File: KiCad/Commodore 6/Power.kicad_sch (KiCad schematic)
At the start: 49 parts, among them J3 Conn_01x05_Pin, Q1 NTR4501NT1G, Q2 PMOS, SW2 SWITCH, SW4 SWITCH, SW6 SWITCH

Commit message: power
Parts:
- removed 1.8LDO: LP5907MFX-1.8, Package_TO_SOT_SMD:SOT-23-5, symbol Regulator_Linear:LP5907MFX-1.8
- removed 2.8LDO: LP5907MFX-2.8, Package_TO_SOT_SMD:SOT-23-5, symbol Regulator_Linear:LP5907MFX-2.8
- removed 3.3LDO: TLV75533PDBV, Package_TO_SOT_SMD:SOT-23-5, symbol Regulator_Linear:TLV75533PDBV
- removed C22, C23, C26, C27, C34, C35: 1uf, symbol Device:C
- removed D1, D3, D4: LED(red), symbol Device:LED
- removed D5: D_Zener_Filled, symbol Device:D_Zener_Filled
- removed DSUB: DA15_Pins, symbol Connector:DA15_Pins
- removed R12, R4: 100R, symbol Device:R
- removed R21: 70R, symbol Device:R
- removed SW2, SW4, SW6: SWITCH, symbol Switch:SW_DPST_x2
- added J4: DE15_Socket_HighDensity_MountingHoles, symbol Connector:DE15_Socket_HighDensity_MountingHoles
- added schottkey: PDS1040L-13, PDS1040L-13:DIO_PDS1040L-13, symbol PDS1040L-13:PDS1040L-13
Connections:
- net 8.4V_evil: now also Q2.1 (D); no longer Q2.3 (S)
- net GND: now also J4.11, J4.12, J4.3, J4.4
- net GNDD: no longer BatteryConnector.2, BatteryConnector.3, C32.1, R13.1, R14.1, R15.1, R16.2
- net RXD: now also J4.15
- net TXD: now also J4.8
- net VOUT: now also BatteryConnector.3, C32.1, R15.1, R16.2, J4.1, J4.10, J4.2, J4.9, schottkey.1, schottkey.2
- net at C33.1, R18.1: now also Q2.3 (S), schottkey.3; no longer Q2.1 (D)
- new net: BatteryConnector.2, R13.1, R14.1
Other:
- added sheet chud ldos (LDOs.kicad_sch)
- moved on the sheet: J3, Q2, TestPoint

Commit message: more
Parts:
- removed C36: 1uF, symbol Device:C
- removed J3: Conn_01x05_Pin, symbol Connector:Conn_01x05_Pin
- removed J4: DE15_Socket_HighDensity_MountingHoles, symbol Connector:DE15_Socket_HighDensity_MountingHoles
- removed TestPoint: GND, symbol Connector:TestPoint
- added C36: WCAP-ASLL_4X5.5/865060640001 1uf smd electrolytic, WCAP-ASLL_4X5.5:WCAP-ASLL_4X5.5_DXL_, symbol WCAP-ASLL_4X5.5:WCAP-ASLL_4X5.5
- added DSUB: ICD15S13E4GX00LF, ICD15S13E4GX00LF:AMPHENOL_ICD15S13E4GX00LF, symbol ICD15S13E4GX00LF:ICD15S13E4GX00LF
- added J6: 6130XX11121_61300511121, 6130XX11121_61300511121:61300511121, symbol 6130XX11121_61300511121:6130XX11121_61300511121
- added R26: RC0402JR-071KL 1k, RC0402N_YAG, symbol 2025-10-26_18-21-17:RC0402JR-071KL
- added TP1: RCWCTE, RCWCTE:TP420X150, symbol RCWCTE:RCWCTE
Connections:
- net 1.8V: now also J6.1
- net 2.8V: now also J6.2
- net 3.3V: now also J6.3
- net 5V: now also C36.1, J6.4
- net 8.4V: now also J6.5
- net GND: now also DSUB.11, DSUB.12, DSUB.3, DSUB.4
- net GNDA: now also TP1.1
- net GNDD: now also C36.2, R26.2
- net RXD: now also DSUB.15
- net TXD: now also DSUB.8
- net VOUT: now also DSUB.1, DSUB.10, DSUB.2, DSUB.9
- net at Payload_Header.2, Payload_LoadSwitch.6 (VOUT): now also R26.1
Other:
- moved on the sheet: Payload_Header

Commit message: AAAAAAAAAA
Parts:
- removed R22: 10k, symbol Device:R
- added C39: WCAP-ASLI_5X5.5/ 47uf electro, WCAP-ASLI_5X5.5:WCAP-ASLI_5X5.5_DXL_, symbol WCAP-ASLI_5X5.5:WCAP-ASLI_5X5.5
- added R27: RC0201FR-0710KL/ 10k, YAG_R0201_YAG, symbol 2025-10-26_02-06-39:RC0201FR-0710KL
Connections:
- net GNDD: now also C39.2, R27.1
- net Payload_Switch: now also R27.2
- net at Payload_Header.2, Payload_LoadSwitch.6 (VOUT), R26.1: now also C39.1
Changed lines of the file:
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@@
 	)
 	(junction
-		(at 130.81 157.48)
+		(at 40.64 39.37)
 		(diameter 0)
 		(color 0 0 0 0)
 	)
 	(junction
-		(at 81.28 34.29)
+		(at 130.81 157.48)
 		(diameter 0)
 		(color 0 0 0 0)
 	)
 	(junction
-		(at 99.06 34.29)
+		(at 81.28 34.29)
 		(diameter 0)
 		(color 0 0 0 0)
 	)
 	(junction
-		(at 40.64 39.37)
+		(at 99.06 34.29)
 		(diameter 0)
 		(color 0 0 0 0)
@@
 	)
 	(junction
+		(at 92.71 34.29)
+		(diameter 0)
+		(color 0 0 0 0)
+	)
+	(junction
 		(at 72.39 154.94)
 		(diameter 0)
@@
 	(wire
 		(pts
+			(xy 92.71 34.29) (xy 99.06 34.29)
+		)
+		(stroke
+			(width 0)
+			(type default)
+		)
+	)
+	(wire
+		(pts
 			(xy 64.77 74.93) (xy 64.77 87.63)
 		)
@@
 	(wire
 		(pts
-			(xy 81.28 34.29) (xy 99.06 34.29)
+			(xy 40.64 52.07) (xy 40.64 53.34)
+		)
+		(stroke
+			(width 0)
+			(type default)
+		)
+	)
+	(wire
+		(pts
+			(xy 81.28 34.29) (xy 92.71 34.29)
 		)
 		(stroke
@@
 	(wire
 		(pts
+			(xy 40.64 39.37) (xy 45.72 39.37)
+		)
+		(stroke
+			(width 0)
+			(type default)
+		)
+	)
+	(wire
+		(pts
 			(xy 72.39 162.56) (xy 72.39 177.8)
 		)
@@
 	(wire
 		(pts
-			(xy 40.64 39.37) (xy 45.72 39.37)
-		)
-		(stroke
-			(width 0)
-			(type default)
-		)
-	)
-	(wire
-		(pts
 			(xy 80.01 157.48) (xy 80.01 167.64)
 		)
@@
 	)
 	(symbol
+		(lib_id "power:GNDD")
+		(at 92.71 41.91 0)
+		(unit 1)
+		(exclude_from_sim no)
+		(in_bom yes)
+		(on_board yes)
+		(dnp no)
+		(fields_autoplaced yes)
+		(property "Reference" "#PWR0105"
+			(at 92.71 48.26 0)
+			(effects
+				(font
+					(size 1.27 1.27)
+				)
+				(hide yes)
+			)
+		)
+		(property "Value" "GNDD"
+			(at 92.71 45.72 0)
+			(effects
+				(font
+					(size 1.27 1.27)
+				)
+			)
+		)
+		(property "Footprint" ""
+			(at 92.71 41.91 0)
+			(effects
+				(font
+					(size 1.27 1.27)
+				)
+				(hide yes)
+			)
+		)
+		(property "Datasheet" ""
+			(at 92.71 41.91 0)
+			(effects
+				(font
+					(size 1.27 1.27)
+				)
+				(hide yes)
+			)
+		)
+		(property "Description" "Power symbol creates a global label with name \"GNDD\" , digital ground"
+			(at 92.71 41.91 0)
+			(effects
+				(font
+					(size 1.27 1.27)
+				)
+				(hide yes)
+			)
+		)
+		(pin "1"
+		)
+		(instances
+			(project "Commodore 6"
+				(path "/27ad1105-577c-4f6a-be9a-9e41c9021a88/0eaef56c-69f1-4e48-a682-2dae5a86159f"
+					(reference "#PWR0105")
+					(unit 1)
+				)
+			)
+		)
+	)
+	(symbol
 		(lib_id "2025-10-26_18-21-17:RC0402JR-071KL")
 		(at 99.06 46.99 90)
@@
 	)
 	(symbol
+		(lib_id "2025-10-26_02-06-39:RC0201FR-0710KL")
+		(at 40.64 52.07 90)
+		(unit 1)
+		(exclude_from_sim no)
+		(in_bom yes)
+		(on_board yes)
+		(dnp no)
+		(property "Reference" "R27"
+			(at 42.418 46.228 90)
+			(effects
+				(font
+					(size 1.524 1.524)
+				)
+				(justify right)
+			)
+		)
+		(property "Value" "RC0201FR-0710KL/ 10k"
+			(at 41.148 49.022 90)
+			(effects
+				(font
+					(size 0.508 0.508)
+				)
+				(justify right)
+			)
+		)
+		(property "Footprint" "YAG_R0201_YAG"
+			(at 40.64 52.07 0)
+			(effects
+				(font
+					(size 1.27 1.27)
+					(italic yes)
+				)
+				(hide yes)
+			)
+		)
+		(property "Datasheet" "RC0201FR-0710KL"
+			(at 40.64 52.07 0)
+			(effects
+				(font
+					(size 1.27 1.27)
+					(italic yes)
+				)
+				(hide yes)
+			)
+		)
+		(property "Description" ""
+			(at 40.64 52.07 0)
+			(effects
+				(font
+					(size 1.27 1.27)
+				)
+				(hide yes)
+			)
+		)
+		(pin "1"
+		)
+		(pin "2"
+		)
+		(instances
+			(project ""
+				(path "/27ad1105-577c-4f6a-be9a-9e41c9021a88/0eaef56c-69f1-4e48-a682-2dae5a86159f"
+					(reference "R27")
+					(unit 1)
+				)
+			)
+		)
+	)
+	(symbol
 		(lib_id "Sensor_Energy:INA219AxD")
 		(at 93.98 92.71 0)
@@
 	(symbol
 		(lib_id "Device:R")
-		(at 40.64 43.18 0)
-		(unit 1)
-		(exclude_from_sim no)
-		(in_bom yes)
-		(on_board yes)
-		(dnp no)
-		(fields_autoplaced yes)
-		(property "Reference" "R22"
-			(at 43.18 41.9099 0)
-			(effects
-				(font
-					(size 1.27 1.27)
-				)
-				(justify left)
-			)
-		)
-		(property "Value" "10k"
-			(at 43.18 44.4499 0)
-			(effects
-				(font
-					(size 1.27 1.27)
-				)
-				(justify left)
-			)
-		)
-		(property "Footprint" ""
-			(at 38.862 43.18 90)
-			(effects
-				(font
-					(size 1.27 1.27)
-				)
-				(hide yes)
-			)
-		)
-		(property "Datasheet" "~"
-			(at 40.64 43.18 0)
-			(effects
-				(font
-					(size 1.27 1.27)
-				)
-				(hide yes)
-			)
-		)
-		(property "Description" "Resistor"
-			(at 40.64 43.18 0)
-			(effects
-				(font
-					(size 1.27 1.27)
-				)
-				(hide yes)
-			)
-		)
-		(pin "1"
-		)
-		(pin "2"
-		)
-		(instances
-			(project ""
-				(path "/27ad1105-577c-4f6a-be9a-9e41c9021a88/0eaef56c-69f1-4e48-a682-2dae5a86159f"
-					(reference "R22")
-					(unit 1)
-				)
-			)
-		)
-	)
-	(symbol
-		(lib_id "Device:R")
 		(at 31.75 101.6 0)
 		(unit 1)
@@
 	(symbol
 		(lib_id "power:GNDD")
-		(at 40.64 46.99 0)
+		(at 40.64 53.34 0)
 		(unit 1)
 		(exclude_from_sim no)
@@
 		(fields_autoplaced yes)
 		(property "Reference" "#PWR086"
-			(at 40.64 53.34 0)
+			(at 40.64 59.69 0)
 			(effects
 				(font
@@
 		)
 		(property "Value" "GNDD"
-			(at 40.64 50.8 0)
+			(at 40.64 57.15 0)
 			(effects
 				(font
@@
 		)
 		(property "Footprint" ""
-			(at 40.64 46.99 0)
+			(at 40.64 53.34 0)
 			(effects
 				(font
@@
 		)
 		(property "Datasheet" ""
-			(at 40.64 46.99 0)
+			(at 40.64 53.34 0)
 			(effects
 				(font
@@
 		)
 		(property "Description" "Power symbol creates a global label with name \"GNDD\" , digital ground"
-			(at 40.64 46.99 0)
+			(at 40.64 53.34 0)
 			(effects
 				(font
@@
 					(unit 1)
 				)
+			)
+		)
+	)
+	(symbol
+		(lib_id "WCAP-ASLI_5X5.5:WCAP-ASLI_5X5.5")
+		(at 92.71 39.37 90)
+		(unit 1)
+		(exclude_from_sim no)
+		(in_bom yes)
+		(on_board yes)
+		(dnp no)
+		(property "Reference" "C39"
+			(at 86.614 38.354 90)
+			(effects
+				(font
+					(size 1.27 1.27)
+				)
+				(justify right)
+			)
+		)
+		(property "Value" "WCAP-ASLI_5X5.5/ 47uf electro"
+			(at 81.026 39.878 90)
+			(effects
+				(font
+					(size 0.4572 0.4572)
+				)
+				(justify right)
+			)
+		)
+		(property "Footprint" "WCAP-ASLI_5X5.5:WCAP-ASLI_5X5.5_DXL_"
+			(at 92.71 39.37 0)
+			(effects
+				(font
+					(size 1.27 1.27)
+				)
+				(justify bottom)
+				(hide yes)
+			)
+		)
+		(property "Datasheet" ""
+			(at 92.71 39.37 0)
+			(effects
+				(font
+					(size 1.27 1.27)
+				)
+				(hide yes)
+			)
+		)
+		(property "Description" ""
+			(at 92.71 39.37 0)
+			(effects
+				(font
+					(size 1.27 1.27)
+				)
+				(hide yes)
+			)
+		)
+		(pin "2"
+		)
+		(pin "1"
+		)
+		(instances
+			(project ""
+				(path "/27ad1105-577c-4f6a-be9a-9e41c9021a88/0eaef56c-69f1-4e48-a682-2dae5a86159f"
+					(reference "C39")
+					(unit 1)
+				)

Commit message: chud
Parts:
- removed R23: 6.8k, symbol Device:R
- removed R24: 3.3k, symbol Device:R
- added R22: ERA-3VRW6801V 6.8k ohm, RES_ERA3V_3K_PAN, symbol 2025-10-26_23-22-38:ERA-3VRW6801V
- added R23: ERA-3VRW3301V 3.3k ohm, RES_ERA3V_3K_PAN, symbol 2025-10-26_23-30-03:ERA-3VRW3301V
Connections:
- net 8.4V: now also R22.2
- net ADC_IN: now also R22.1, R23.2
- net GNDD: now also R23.1
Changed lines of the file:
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@@
 	(text "2.744V\n"
 		(exclude_from_sim no)
-		(at 26.67 93.98 0)
+		(at 26.924 97.536 0)
 		(effects
 			(font
@@
 	)
 	(junction
+		(at 31.75 96.52)
+		(diameter 0)
+		(color 0 0 0 0)
+	)
+	(junction
 		(at 93.98 72.39)
 		(diameter 0)
@@
 	(wire
 		(pts
-			(xy 31.75 77.47) (xy 31.75 81.28)
+			(xy 31.75 96.52) (xy 31.75 99.06)
 		)
 		(stroke
@@
 	(wire
 		(pts
-			(xy 31.75 97.79) (xy 31.75 88.9)
+			(xy 34.29 96.52) (xy 31.75 96.52)
 		)
 		(stroke
@@
 	(wire
 		(pts
+			(xy 31.75 90.17) (xy 31.75 96.52)
+		)
+		(stroke
+			(width 0)
+			(type default)
+		)
+	)
+	(wire
+		(pts
 			(xy 64.77 87.63) (xy 83.82 87.63)
 		)
@@
 	(global_label "ADC_IN"
 		(shape input)
-		(at 31.75 93.98 0)
+		(at 34.29 96.52 0)
 		(fields_autoplaced yes)
 		(effects
@@
 		)
 		(property "Intersheetrefs" "${INTERSHEET_REFS}"
-			(at 41.2667 93.98 0)
+			(at 43.8067 96.52 0)
 			(effects
 				(font
@@
 	)
 	(symbol
-		(lib_id "Device:R")
-		(at 31.75 101.6 0)
+		(lib_id "2025-10-26_23-30-03:ERA-3VRW3301V")
+		(at 31.75 111.76 90)
 		(unit 1)
 		(exclude_from_sim no)
@@
 		(dnp no)
 		(fields_autoplaced yes)
-		(property "Reference" "R24"
-			(at 34.29 100.3299 0)
+		(property "Reference" "R23"
+			(at 34.29 104.7749 90)
 			(effects
 				(font
-					(size 1.27 1.27)
+					(size 1.524 1.524)
 				)
-				(justify left)
+				(justify right)
 			)
 		)
-		(property "Value" "3.3k"
-			(at 34.29 102.8699 0)
+		(property "Value" "ERA-3VRW3301V 3.3k ohm"
+			(at 34.29 106.68 90)
 			(effects
 				(font
-					(size 1.27 1.27)
+					(size 0.508 0.508)
 				)
-				(justify left)
+				(justify right)
 			)
 		)
-		(property "Footprint" ""
-			(at 29.972 101.6 90)
+		(property "Footprint" "RES_ERA3V_3K_PAN"
+			(at 31.75 111.76 0)
 			(effects
 				(font
 					(size 1.27 1.27)
+					(italic yes)
 				)
 				(hide yes)
 			)
 		)
-		(property "Datasheet" "~"
-			(at 31.75 101.6 0)
+		(property "Datasheet" "ERA-3VRW3301V"
+			(at 31.75 111.76 0)
 			(effects
 				(font
 					(size 1.27 1.27)
+					(italic yes)
 				)
 				(hide yes)
 			)
 		)
-		(property "Description" "Resistor"
-			(at 31.75 101.6 0)
+		(property "Description" ""
+			(at 31.75 111.76 0)
 			(effects
 				(font
@@
 		)
 		(instances
-			(project "Commodore 6"
+			(project ""
 				(path "/27ad1105-577c-4f6a-be9a-9e41c9021a88/0eaef56c-69f1-4e48-a682-2dae5a86159f"
-					(reference "R24")
+					(reference "R23")
 					(unit 1)
 				)
@@
 	)
 	(symbol
-		(lib_id "Device:R")
-		(at 31.75 85.09 0)
+		(lib_id "2025-10-26_23-22-38:ERA-3VRW6801V")
+		(at 31.75 90.17 90)
 		(unit 1)
 		(exclude_from_sim no)
@@
 		(dnp no)
 		(fields_autoplaced yes)
-		(property "Reference" "R23"
-			(at 34.29 83.8199 0)
+		(property "Reference" "R22"
+			(at 34.29 83.1849 90)
 			(effects
 				(font
-					(size 1.27 1.27)
+					(size 1.524 1.524)
 				)
-				(justify left)
+				(justify right)
 			)
 		)
-		(property "Value" "6.8k"
-			(at 34.29 86.3599 0)
+		(property "Value" "ERA-3VRW6801V 6.8k ohm"
+			(at 34.29 85.09 90)
 			(effects
 				(font
-					(size 1.27 1.27)
+					(size 0.508 0.508)
 				)
-				(justify left)
+				(justify right)
 			)
 		)
-		(property "Footprint" ""
-			(at 29.972 85.09 90)
+		(property "Footprint" "RES_ERA3V_3K_PAN"
+			(at 31.75 90.17 0)
 			(effects
 				(font
 					(size 1.27 1.27)
+					(italic yes)
 				)
 				(hide yes)
 			)
 		)
-		(property "Datasheet" "~"
-			(at 31.75 85.09 0)
+		(property "Datasheet" "ERA-3VRW6801V"
+			(at 31.75 90.17 0)
 			(effects
 				(font
 					(size 1.27 1.27)
+					(italic yes)
 				)
 				(hide yes)
 			)
 		)
-		(property "Description" "Resistor"
-			(at 31.75 85.09 0)
+		(property "Description" ""
+			(at 31.75 90.17 0)
 			(effects
 				(font
@@
 			(project ""
 				(path "/27ad1105-577c-4f6a-be9a-9e41c9021a88/0eaef56c-69f1-4e48-a682-2dae5a86159f"
-					(reference "R23")
+					(reference "R22")
 					(unit 1)
 				)
@@
 	(symbol
 		(lib_id "power:GNDD")
-		(at 31.75 105.41 0)
+		(at 31.75 111.76 0)
 		(unit 1)
 		(exclude_from_sim no)
@@
 		(fields_autoplaced yes)
 		(property "Reference" "#PWR095"
-			(at 31.75 111.76 0)
+			(at 31.75 118.11 0)
 			(effects
 				(font
@@
 		)
 		(property "Value" "GNDD"
-			(at 31.75 109.22 0)
+			(at 31.75 115.57 0)
 			(effects
 				(font
@@
 		)
 		(property "Footprint" ""
-			(at 31.75 105.41 0)
+			(at 31.75 111.76 0)
 			(effects
 				(font
@@
 		)
 		(property "Datasheet" ""
-			(at 31.75 105.41 0)
+			(at 31.75 111.76 0)
 			(effects
 				(font
@@
 		)
 		(property "Description" "Power symbol creates a global label with name \"GNDD\" , digital ground"
-			(at 31.75 105.41 0)
+			(at 31.75 111.76 0)
 			(effects
 				(font

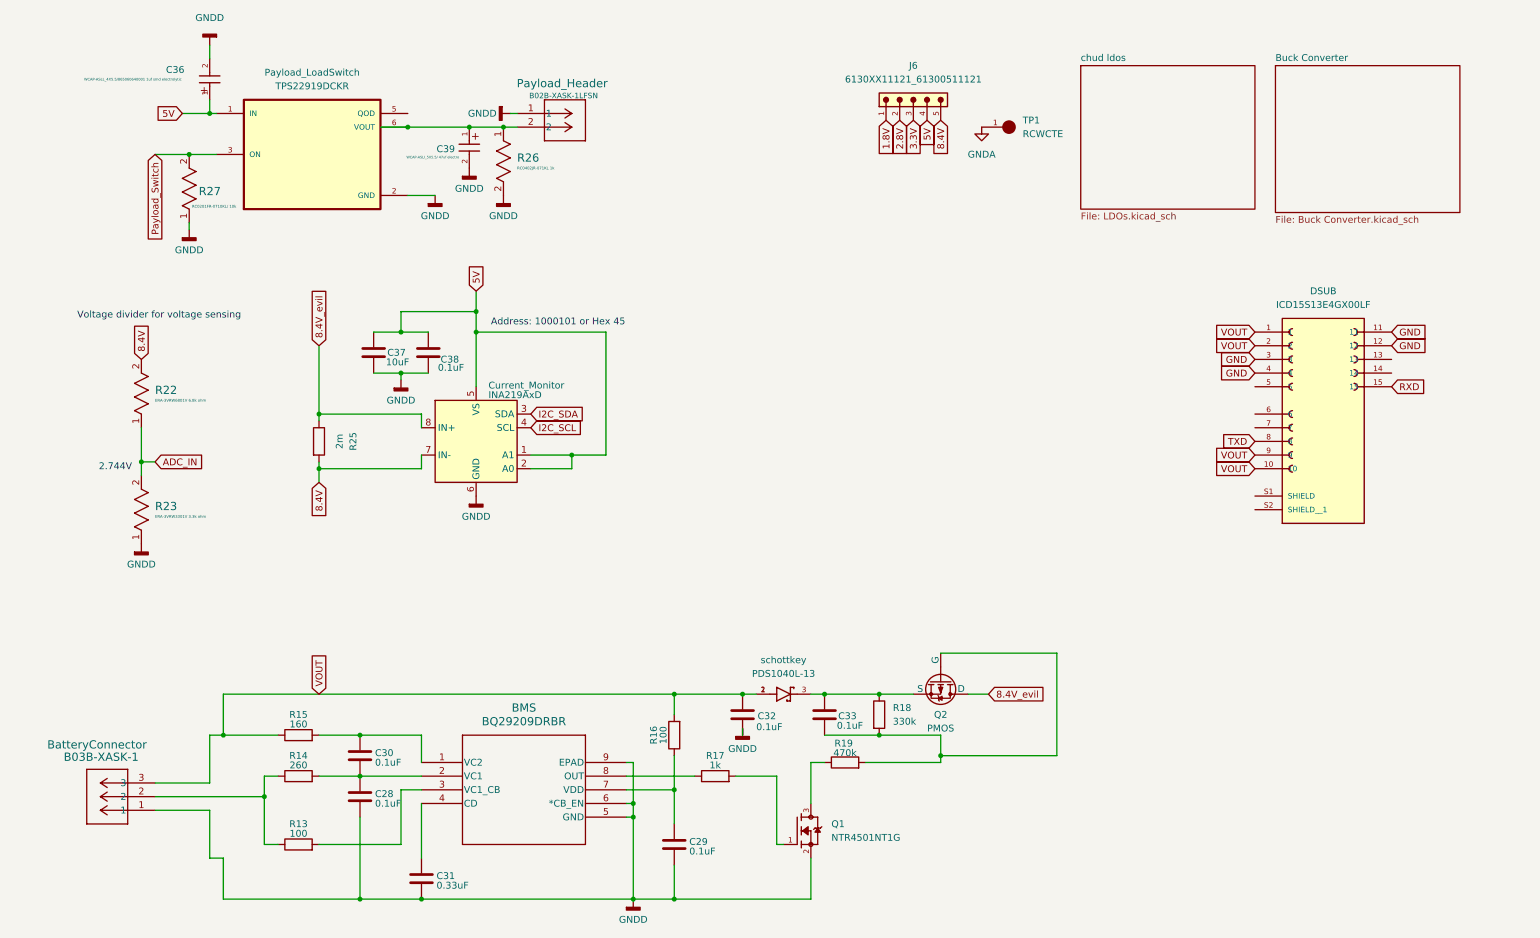
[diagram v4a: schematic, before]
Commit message: Adding Footprints
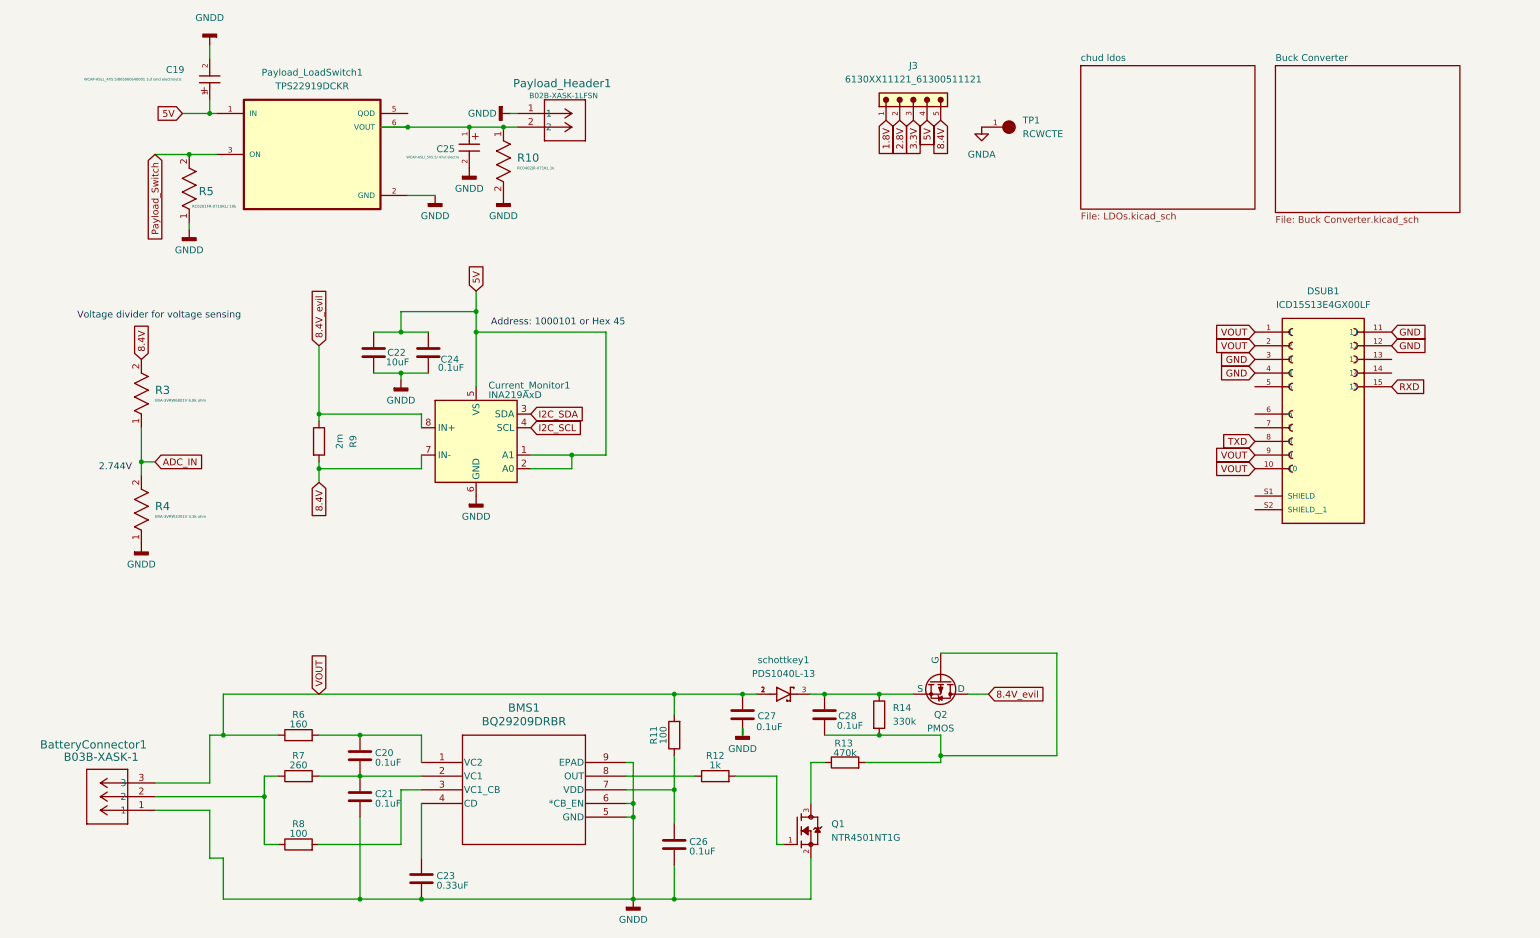
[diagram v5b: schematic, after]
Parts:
- BMS1: renamed from BMS; footprint DRB8_1P6X2P4 -> (none)
- BatteryConnector1: renamed from BatteryConnector; footprint CONN_B03B-XASK-1_JST -> (none)
- C20: renamed from C30; footprint (none) -> Capacitor_SMD:C_1206_3216Metric
- C21: renamed from C28; footprint (none) -> Capacitor_SMD:C_1206_3216Metric
- C22: renamed from C37; footprint (none) -> Capacitor_SMD:C_1206_3216Metric
- C23: renamed from C31; footprint (none) -> Capacitor_SMD:C_1206_3216Metric
- C24: renamed from C38; footprint (none) -> Capacitor_SMD:C_1206_3216Metric
- C26: renamed from C29; footprint (none) -> Capacitor_SMD:C_1206_3216Metric
- C27: renamed from C32; footprint (none) -> Capacitor_SMD:C_1206_3216Metric
- C28: renamed from C33; footprint (none) -> Capacitor_SMD:C_1206_3216Metric
- Payload_Header1: renamed from Payload_Header; footprint CONN_B02B-XASK-1LFSN_JST -> (none)
- R10: renamed from R26; footprint RC0402N_YAG -> (none)
- R11: renamed from R16; footprint (none) -> Resistor_SMD:R_1206_3216Metric
- R12: renamed from R17; footprint (none) -> Resistor_SMD:R_1206_3216Metric
- R13: renamed from R19; footprint (none) -> Resistor_SMD:R_1206_3216Metric
- R14: renamed from R18; footprint (none) -> Resistor_SMD:R_1206_3216Metric
- R3: renamed from R22; footprint RES_ERA3V_3K_PAN -> (none)
- R4: renamed from R23; footprint RES_ERA3V_3K_PAN -> (none)
- R5: renamed from R27; footprint YAG_R0201_YAG -> (none)
- R6: renamed from R15; footprint (none) -> Resistor_SMD:R_1206_3216Metric
- R7: renamed from R14; footprint (none) -> Resistor_SMD:R_1206_3216Metric
- R8: renamed from R13; footprint (none) -> Resistor_SMD:R_1206_3216Metric
- R9: renamed from R25; footprint (none) -> Resistor_SMD:R_1206_3216Metric
- renumbered C36 to C19, C39 to C25, Current_Monitor to Current_Monitor1, DSUB to DSUB1, J6 to J3, Payload_LoadSwitch to Payload_LoadSwitch1, schottkey to schottkey1
